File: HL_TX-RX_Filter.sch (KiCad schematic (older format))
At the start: 210 parts, among them J1 CNR1, J10 SCL SDA, J11 To Rx in, J12 CONN_01X03, J2 CNR3, J3 Antenna, J4 CNR2, J5 CNR4, J6 From Tx, J7 + - 12v, J8 ICSP, J9 CONN_01X05, Q1 2N7002, Q2 2N7002, Q3 2N7002, Q4 2N7002, Q5 2N7002, Q6 2N7002, Q7 2N7002, Q8 2N7002, U1 ATMEGA328-AU, U10 PE4259, U11 PE4259, U12 PE4259, U2 PE4259, U3 PE4259, U4 PE4259, U5 PE4259, U6 PE4259, U7 PE4259, U8 PE4259, U9 PE4259

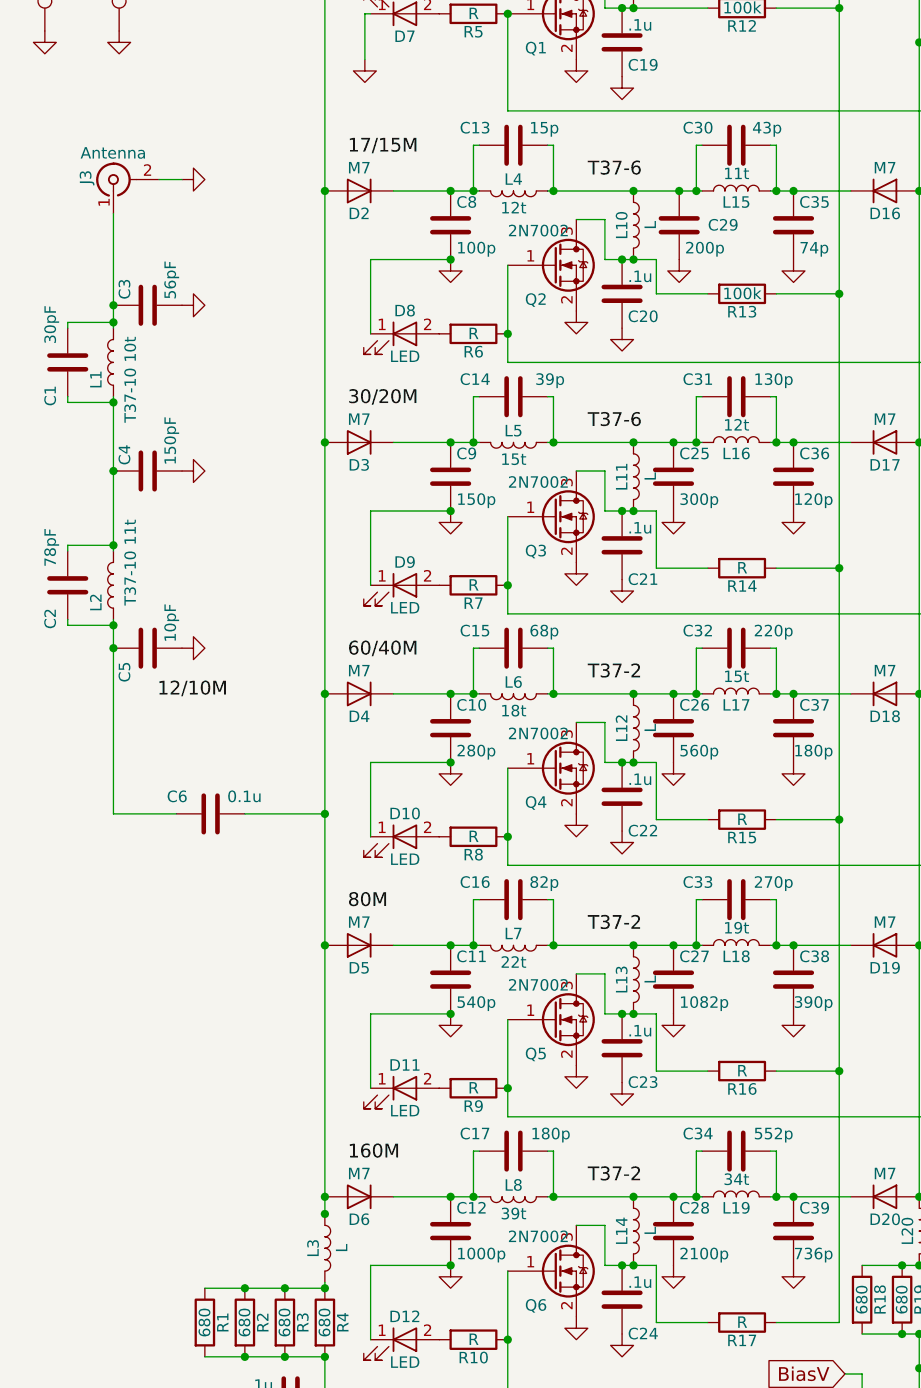
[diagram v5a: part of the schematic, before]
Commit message: Corrections to filter values
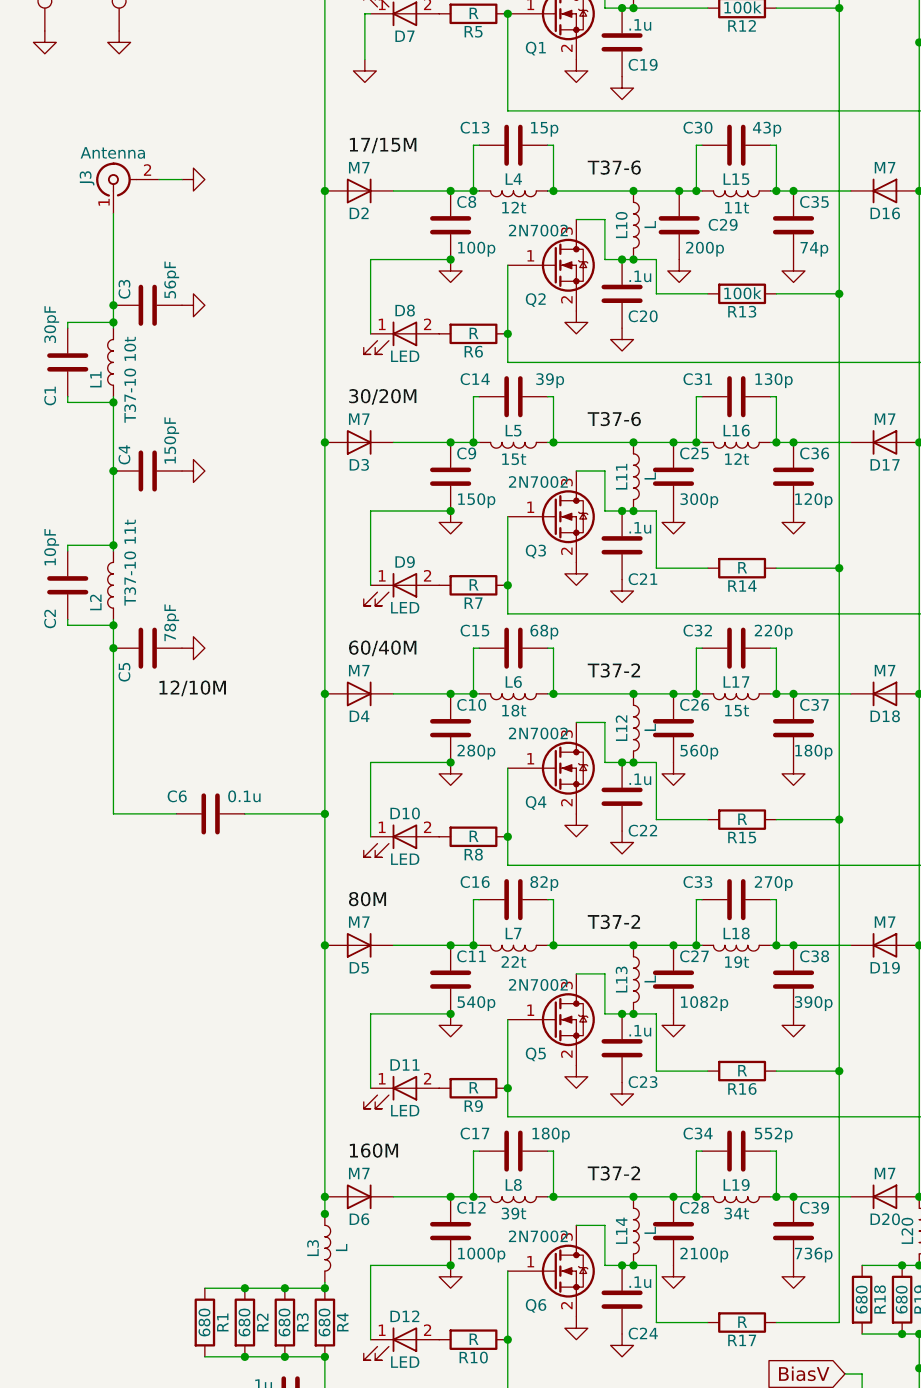
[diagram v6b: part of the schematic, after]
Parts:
- C2: value 78pF -> 10pF
- C5: value 10pF -> 78pF
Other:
- moved on the sheet: L15, L16, L17, L18, L19
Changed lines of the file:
@@
 F 3 "" H 3750 6625 50  0001 C CNN
 	1    3750 6625
-	0    -1   -1   0
+	0    -1   1    0
 $EndComp
 $Comp
@@
 F 3 "" H 3750 5525 50  0001 C CNN
 	1    3750 5525
-	0    -1   -1   0
+	0    -1   1    0
 $EndComp
 $Comp
@@
 F 3 "" H 3750 4425 50  0001 C CNN
 	1    3750 4425
-	0    -1   -1   0
+	0    -1   1    0
 $EndComp
 $Comp
@@
 F 3 "" H 3750 3325 50  0001 C CNN
 	1    3750 3325
-	0    -1   -1   0
+	0    -1   1    0
 $EndComp
 $Comp
@@
 F 3 "" H 3750 2225 50  0001 C CNN
 	1    3750 2225
-	0    -1   -1   0
+	0    -1   1    0
 $EndComp
 $Comp
@@
 P 825 3950
 F 0 "C2" V 900 4050 50  0000 L CNN
-F 1 "78pF" V 900 3700 50  0000 L CNN
+F 1 "10pF" V 900 3700 50  0000 L CNN
 F 2 "Capacitors_SMD:C_1206_HandSoldering" H 863 3800 50  0001 C CNN
 F 3 "" H 825 3950 50  0001 C CNN
@@
 P 1175 4225
 F 0 "C5" H 1025 4325 50  0000 L CNN
-F 1 "10pF" H 1200 4125 50  0000 L CNN
+F 1 "78pF" H 1200 4125 50  0000 L CNN
 F 2 "Capacitors_SMD:C_1206_HandSoldering" H 1213 4075 50  0001 C CNN
 F 3 "" H 1175 4225 50  0001 C CNN
